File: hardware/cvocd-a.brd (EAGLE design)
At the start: 152.5 x 43.6 mm, 71 parts, among them IC1 PIC16F1825SO14, IC2 74HC595D, IC3 74HC595D, IC4 MCP4728_QUAD_DAC, IC5 LM324D, IC6 REG1117, IC7 6N138

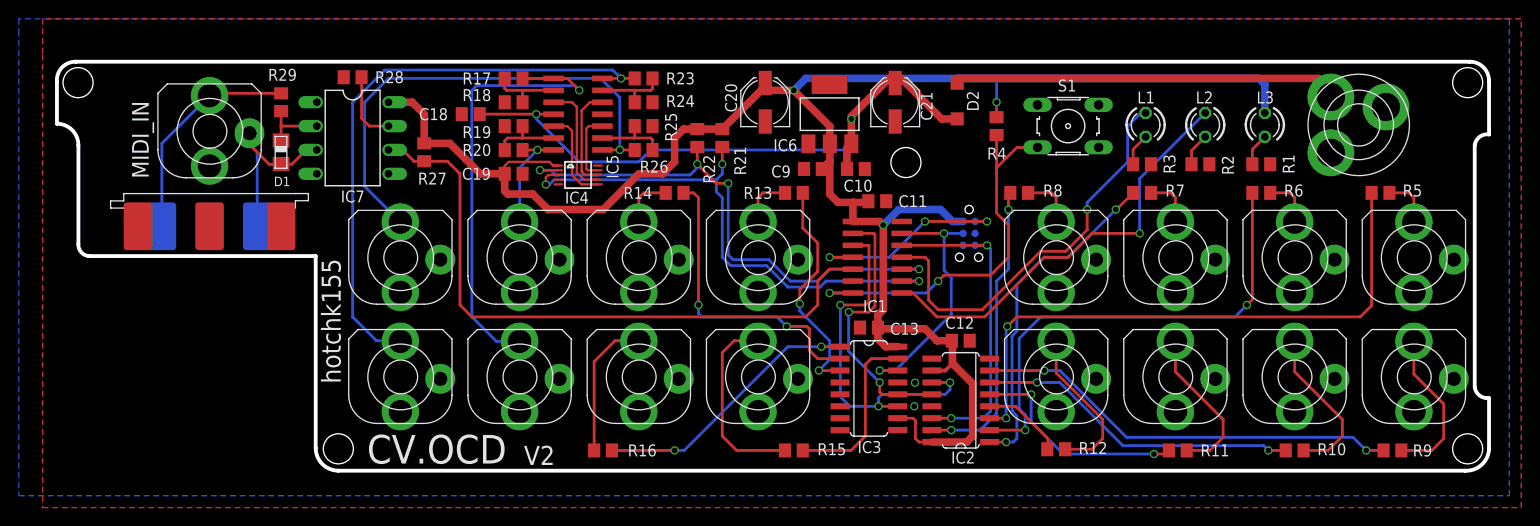
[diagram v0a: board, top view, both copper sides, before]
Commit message: icsp to top layer, current lim resistors
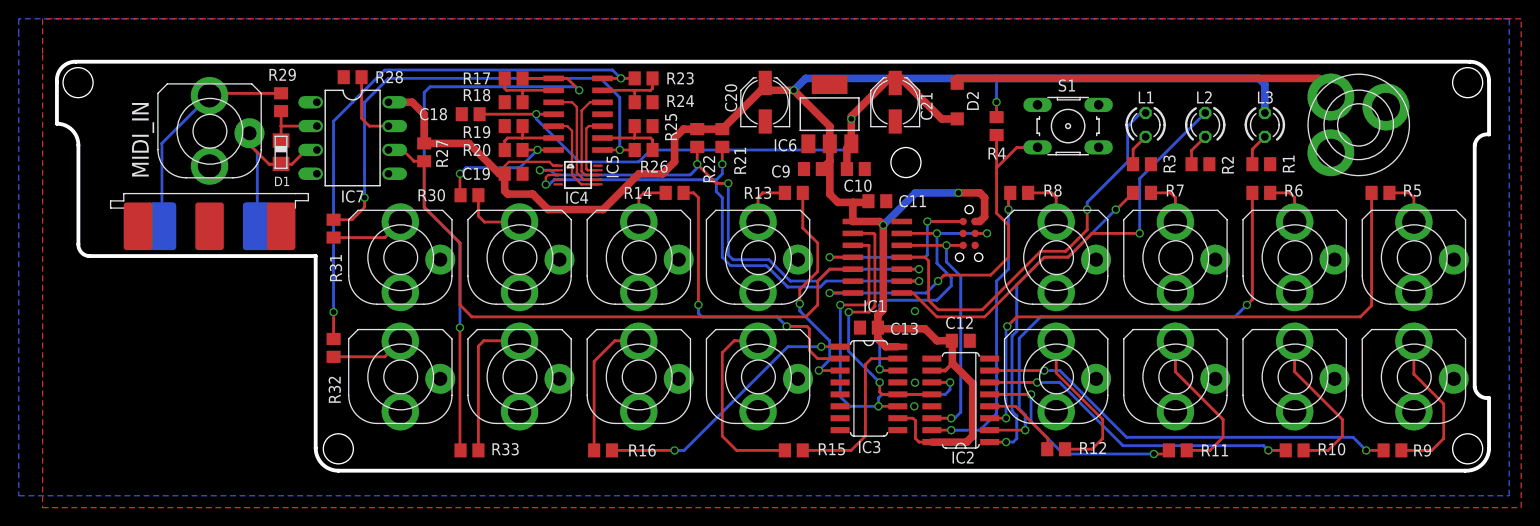
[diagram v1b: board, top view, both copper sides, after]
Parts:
- added R30, R31, R32, R33: 220r, rcl:R0805
- flipped ICSP to the top
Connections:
- new net N$10: CVD.4, R33.2
- new net N$11: CVB.4, R30.2
- new net N$14: CVA.4, R31.2
- new net N$17: CVC.4, R32.2
- net N$2: now also R33.1; no longer CVD.4
- net N$3: now also R30.1; no longer CVB.4
- net N$4: now also R31.1; no longer CVA.4
- net N$5: now also R32.1; no longer CVC.4
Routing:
- net N$10: track 0.00 -> 15.8 mm
- net N$2: track 48.7 -> 63.2 mm, vias 1 -> 2
- net N$17: track 0.00 -> 7.80 mm
- net N$14: track 0.00 -> 7.80 mm
- net N$11: track 0.00 -> 6.87 mm
- net SR_DAT2: track 34.7 -> 28.3 mm
- net SR_DAT: track 27.5 -> 33.9 mm, vias 2 -> 3
- net VDD: track 204.4 -> 210.4 mm, vias 3 -> 4
- net N$3: track 11.8 -> 14.9 mm, vias 1 -> 2
- net N$5: track 62.8 -> 59.9 mm, vias 1 -> 2
- net N$34: track 22.1 -> 20.4 mm, vias 3 -> 2
- net MIDI_IN: track 68.6 -> 67.2 mm
- net N$4: track 52.4 -> 53.1 mm, vias 1 -> 2
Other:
- board text added: "CC-NC-BY-SA"
- board text added: "V3"
- board text removed: "CV.OCD"
- board text removed: "V2"

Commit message: V3 possible final..
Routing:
- net N$33: track 16.9 -> 13.5 mm
- net GND: track 0.00 -> 3.11 mm, vias 3 -> 6
- net N$34: track 20.4 -> 19.8 mm
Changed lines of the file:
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@@
 </class>
 </classes>
-<designrules name="dirt_cheap_dirty_boards.v1">
-<description language="en">&lt;b&gt;Dirty Cheap Dirty Board Design Rules&lt;/b&gt;
-&lt;br&gt;
-&lt;br&gt;Min width/Spacing: 5/5mil
-&lt;br&gt;Min diameter of finished hole 12mil</description>
+<designrules name="hackvana">
+<description language="de">&lt;b&gt;EAGLE Design Rules für Hackvana&lt;/b&gt;
+&lt;p&gt;
+Die Standard-Design-Rules sind so gewählt, dass sie für
+die meisten Anwendungen passen. Sollte ihre Platine
+besondere Anforderungen haben, treffen Sie die erforderlichen
+Einstellungen hier und speichern die Design Rules unter
+einem neuen Namen ab.</description>
+<description language="en">&lt;b&gt;EAGLE Design Rules for Hackvana&lt;/b&gt;
+&lt;p&gt;
+The default Design Rules have been set to cover
+a wide range of applications. Your particular design
+may have different requirements, so please make the
+necessary adjustments and save your customized
+design rules under a new name.</description>
+<description language="zh">&lt;b&gt;EAGLE Design Rules for Hackvana&lt;/b&gt;
+</description>
 <param name="layerSetup" value="(1*16)"/>
-<param name="mtCopper" value="0.035mm 0.0175mm 0.035mm 0.035mm 0.035mm 0.035mm 0.035mm 0.035mm 0.035mm 0.035mm 0.035mm 0.035mm 0.035mm 0.035mm 0.0175mm 0.035mm"/>
-<param name="mtIsolate" value="1.5mm 1.1mm 0.2mm 0.15mm 0.2mm 0.15mm 0.2mm 0.15mm 0.2mm 0.15mm 0.2mm 0.15mm 0.2mm 0.15mm 0.2mm"/>
-<param name="mdWireWire" value="5mil"/>
-<param name="mdWirePad" value="5mil"/>
-<param name="mdWireVia" value="5mil"/>
-<param name="mdPadPad" value="5mil"/>
-<param name="mdPadVia" value="5mil"/>
-<param name="mdViaVia" value="5mil"/>
+<param name="mtCopper" value="0.035mm 0.035mm 0.035mm 0.035mm 0.035mm 0.035mm 0.035mm 0.035mm 0.035mm 0.035mm 0.035mm 0.035mm 0.035mm 0.035mm 0.035mm 0.035mm"/>
+<param name="mtIsolate" value="1.5mm 0.15mm 0.2mm 0.15mm 0.2mm 0.15mm 0.2mm 0.15mm 0.2mm 0.15mm 0.2mm 0.15mm 0.2mm 0.15mm 0.2mm"/>
+<param name="mdWireWire" value="6mil"/>
+<param name="mdWirePad" value="9mil"/>
+<param name="mdWireVia" value="6mil"/>
+<param name="mdPadPad" value="6mil"/>
+<param name="mdPadVia" value="6mil"/>
+<param name="mdViaVia" value="6mil"/>
 <param name="mdSmdPad" value="0mil"/>
 <param name="mdSmdVia" value="0mil"/>
@@
 <param name="mdViaViaSameLayer" value="8mil"/>
 <param name="mnLayersViaInSmd" value="2"/>
-<param name="mdCopperDimension" value="10mil"/>
-<param name="mdDrill" value="10mil"/>
+<param name="mdCopperDimension" value="6mil"/>
+<param name="mdDrill" value="6mil"/>
 <param name="mdSmdStop" value="0mil"/>
-<param name="msWidth" value="5mil"/>
-<param name="msDrill" value="12mil"/>
-<param name="msMicroVia" value="12mil"/>
+<param name="msWidth" value="6mil"/>
+<param name="msDrill" value="0.3mm"/>
+<param name="msMicroVia" value="0.25mm"/>
 <param name="msBlindViaRatio" value="0.5"/>
 <param name="rvPadTop" value="0.25"/>
@@
 <param name="mlMinCreamFrame" value="0mil"/>
 <param name="mlMaxCreamFrame" value="0mil"/>
-<param name="mlViaStopLimit" value="25mil"/>
+<param name="mlViaStopLimit" value="100mil"/>
 <param name="srRoundness" value="0"/>
 <param name="srMinRoundness" value="0mil"/>
@@
 <element name="U$2" library="jason_eagle6" package="PWR_SOCKET_2_1MM" value="PWR_SOCKET_2_1MM" x="138.905" y="35.687" smashed="yes" rot="R45"/>
 <element name="C21" library="rcl" package="PANASONIC_C" value="" x="89.535" y="38.1" smashed="yes" rot="R90">
-<attribute name="NAME" x="93.516" y="36.135" size="1.27" layer="25" rot="R90"/>
+<attribute name="NAME" x="93.77" y="36.77" size="1.27" layer="25" rot="R90"/>
 <attribute name="VALUE" x="93.31" y="35.45" size="1.016" layer="27" rot="R90"/>
 </element>
@@
 <via x="91.6432" y="8.2296" extent="1-16" drill="0.6"/>
 <via x="91.6432" y="15.8496" extent="1-16" drill="0.6"/>
+<via x="109.8042" y="1.6256" extent="1-16" drill="0.6"/>
+<via x="110.9472" y="1.6256" extent="1-16" drill="0.6"/>
+<via x="112.0902" y="1.6256" extent="1-16" drill="0.6"/>
+<wire x1="53.6399" y1="29.853" x2="54.729" y2="29.853" width="0.254" layer="1"/>
+<wire x1="54.729" y1="29.853" x2="54.864" y2="29.718" width="0.254" layer="1"/>
+<wire x1="54.864" y1="29.718" x2="54.864" y2="29.464" width="0.254" layer="1"/>
+<wire x1="57.8661" y1="31.353" x2="59.42" y2="31.353" width="0.254" layer="1"/>
+<wire x1="59.42" y1="31.353" x2="59.436" y2="31.369" width="0.254" layer="1"/>
 </signal>
 <signal name="N$1">
@@
 <contactref element="IC1" pad="4"/>
 <contactref element="ICSP" pad="1"/>
-<via x="92.964" y="25.4" extent="1-16" drill="0.6"/>
+<via x="95.504" y="25.4" extent="1-16" drill="0.6"/>
 <via x="82.55" y="21.59" extent="1-16" drill="0.6"/>
 <wire x1="82.55" y1="21.59" x2="85.03" y2="21.59" width="0.3048" layer="1"/>
 <wire x1="92.71" y1="21.59" x2="82.55" y2="21.59" width="0.3048" layer="16"/>
-<wire x1="92.964" y1="25.4" x2="96.774" y2="25.4" width="0.3048" layer="1"/>
-<wire x1="92.964" y1="25.4" x2="92.964" y2="21.844" width="0.3048" layer="16"/>
+<wire x1="95.504" y1="25.4" x2="96.774" y2="25.4" width="0.3048" layer="1"/>
 <wire x1="92.964" y1="21.844" x2="92.71" y2="21.59" width="0.3048" layer="16"/>
+<wire x1="92.964" y1="21.844" x2="92.964" y2="24.511" width="0.3048" layer="16"/>
+<wire x1="95.504" y1="25.4" x2="93.853" y2="25.4" width="0.3048" layer="16"/>
+<wire x1="93.853" y1="25.4" x2="92.964" y2="24.511" width="0.3048" layer="16"/>
 </signal>
 <signal name="N$35">
@@
 <contactref element="R4" pad="1"/>
 <contactref element="C20" pad="+"/>
-<wire x1="53.6399" y1="31.353" x2="53.229" y2="31.353" width="0.3048" layer="1"/>
-<wire x1="53.229" y1="31.353" x2="53.102" y2="31.353" width="0.254" layer="1"/>
 <wire x1="53.102" y1="31.353" x2="52.705" y2="31.75" width="0.254" layer="1"/>
 <wire x1="52.705" y1="31.75" x2="48.387" y2="31.75" width="0.254" layer="1"/>
@@
 <wire x1="88.265" y1="25.019" x2="91.694" y2="28.448" width="0.8128" layer="16"/>
 <wire x1="91.694" y1="28.448" x2="96.266" y2="28.448" width="0.8128" layer="16"/>
+<wire x1="53.102" y1="31.353" x2="53.6399" y2="31.353" width="0.254" layer="1"/>
 </signal>
 <signal name="VIN">
@@
 <contactref element="GATE9" pad="4"/>
 <wire x1="106.68" y1="12.64" x2="106.68" y2="9.271" width="0.3048" layer="1"/>
-<wire x1="106.68" y1="9.271" x2="111.633" y2="4.318" width="0.3048" layer="1"/>
-<wire x1="111.633" y1="4.318" x2="111.633" y2="2.286" width="0.3048" layer="1"/>
-<wire x1="111.633" y1="2.286" x2="110.49" y2="1.143" width="0.3048" layer="1"/>
-<wire x1="110.49" y1="1.143" x2="107.63" y2="1.143" width="0.3048" layer="1"/>
+<wire x1="106.68" y1="9.271" x2="109.601" y2="6.35" width="0.3048" layer="1"/>
+<wire x1="109.601" y1="6.35" x2="109.601" y2="3.114" width="0.3048" layer="1"/>
+<wire x1="109.601" y1="3.114" x2="107.63" y2="1.143" width="0.3048" layer="1"/>
 </signal>
 <signal name="N$39">

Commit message: working on v4
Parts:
- removed C10: (no value), rcl:C0805
- removed C18, C19, C9: 100n, rcl:C0805
- removed C20, C21: (no value), rcl:PANASONIC_C
- added C1, C4: 100n, rcl:C0805
- added C2, C3: (no value), rcl:PANASONIC_C
- added C5: (no value), rcl:C0805
- added PA, PB, PC, PD: (no value), rcl:RTRIM3314G
- IC1: value PIC16F1825SO14 -> 6N138; device jasons_stuff:SO14 -> optocoupler:DIL08
- IC2: value 74HC595D -> LM324D; device 74xx-eu:SO16 -> linear:SO14
- IC3: value 74HC595D -> MCP4728_QUAD_DAC; device 74xx-eu:SO16 -> jason_eagle6:MSOP10
- IC4: value MCP4728_QUAD_DAC -> REG1117; device jason_eagle6:MSOP10 -> burr-brown:SOT223
- IC5: value LM324D -> PIC16F1825SO14; device linear:SO14 -> jasons_stuff:SO14
- IC6: value REG1117 -> 74HC595D; device burr-brown:SOT223 -> 74xx-eu:SO16
- IC7: value 6N138 -> 74HC595D; device optocoupler:DIL08 -> 74xx-eu:SO16
- R10, R11, R8, R9: value (none) -> 220r
- R12, R13, R14, R15, R5, R6, R7: value (none) -> 100k
- R17, R18, R19, R23, R24, R25, R26: value 100k -> (none)
- R2, R3: value (none) -> 1k5
- R20: value 100k -> 4k7
- R22: value 4k7 -> 10k
- R27, R28: value 1k5 -> (none)
- R30, R31, R32, R33: value 220r -> (none)
- R4: value 10k -> 100k
- moved R1 119.8 mm to (8.89, 38.1), turned to 270 degrees
- moved R29 117.5 mm to (141.2, 28.4), turned to 0 degrees
- moved R32 102.9 mm to (132.1, 1.02), turned to 0 degrees
- moved R9 98.3 mm to (49.9, 34.2), turned to 90 degrees
- moved R33 98.3 mm to (142.5, 1.02)
- moved R28 97.6 mm to (128.5, 28.4), turned to 0 degrees
- moved R2 96.2 mm to (26.3, 40.6), turned to 180 degrees
- moved R5 95.1 mm to (46.6, 38.2)
- moved R31 93.0 mm to (119.6, 1.02), turned to 0 degrees
- moved R3 84.2 mm to (32.1, 40.6)
- moved R6 82.2 mm to (46.6, 35.3), turned to 180 degrees
- moved R10 80.1 mm to (61.7, 39.2), turned to 270 degrees
- moved R27 76.6 mm to (115.8, 28.4), turned to 0 degrees
- moved IC7 70.5 mm to (96.5, 6.35), turned to 90 degrees
- moved R7 69.4 mm to (46.6, 32.9)
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- renumbered C11 to C6, C12 to C8, C13 to C7, L1 to LED1, L2 to LED2, L3 to LED3, S1 to SW1
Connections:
- removed net N$3 (its old number): IC5.7, R20.2, R30.1
- new net N$18: CVD.4, R5.2, R8.2
- new net N$19: CVB.4, R7.2, R9.2
- new net N$38: CVA.4, R11.2, R14.2
- new net N$44: CVC.4, R10.2, R12.2
- new net N$45: PA.1, R15.2
- new net N$53: IC7.7, R33.1
- new net N$54: PA.3, R14.1
- new net N$55: PC.1, R13.2
- new net N$56: PC.3, R12.1
- net ACT_LED: now also IC5.11; no longer IC1.11
- net GND: now also C1.1, C2.-, C3.-, C4.1, C5.1, IC1.5, IC2.11, IC3.10, IC3.4, IC4.1, IC5.14, IC6.13, IC6.8, IC7.13, IC7.8, R13.1, R15.1, R23.2, R24.2, R25.2, R4.1, R6.1; no longer C10.1, C18.2, C19.1, C20.-, C21.-, C9.1, IC1.14, IC2.13, IC2.8, IC3.13, IC3.8, IC4.10, IC4.4, IC5.11, IC6.1, IC7.5, R1.2, R18.1, R19.1, R2.2, R24.1, R25.1, R28.2
- net MIDI_IN: now also IC1.6, IC5.5, R2.1; no longer IC1.5, IC7.6, R27.1
- net MIDI_OUT: now also IC5.6; no longer IC1.6
- net N$1: now also R19.2; no longer R15.2
- net N$10: now also IC2.2, PD.2; no longer CVD.4, R33.2
- net N$11: now also IC2.9, PA.2; no longer CVB.4, R30.2
- net N$12: now also IC6.15, R19.1; no longer IC3.15, R15.1
- net N$13: now also IC6.1, R18.1; no longer IC3.1, R16.1
- net N$14: now also IC2.13, PC.2; no longer CVA.4, R31.2
- net N$15: now also IC6.3, R17.1; no longer IC3.3, R13.1
- net N$16: now also IC6.2, R16.1; no longer IC3.2, R14.1
- net N$17: now also PD.1, R4.2; no longer CVC.4, R32.2
- net N$2: now also IC2.1, R8.1; no longer IC5.1, R17.2, R33.1
- net N$20: now also R26.2; no longer R8.2
- net N$21: now also IC3.2, IC5.10, R21.2; no longer IC1.10, IC4.2, R22.2
- net N$22: now also IC3.3, IC5.9, R20.2; no longer IC1.9, IC4.3, R21.2
- net N$23: now also R27.2; no longer R7.2
- net N$24: now also R28.2; no longer R6.2
- net N$25: now also PD.3, R5.1; no longer IC5.2, R17.1, R18.2
- net N$26: now also IC2.6, PB.2; no longer IC5.6, R19.2, R20.1
- net N$27: now also PB.1, R6.2; no longer IC5.9, R25.2, R26.1
- net N$28: now also PB.3, R7.1; no longer IC5.13, R23.1, R24.2
- net N$29: now also R1.1; no longer R29.1
- net N$30: now also IC1.2, R1.2; no longer IC7.2, R29.2
- net N$31: now also IC1.3; no longer IC7.3
- net N$32: now also R29.2; no longer R5.2
- net N$33: now also R30.2; no longer R12.2
- net N$34: now also IC5.4; no longer IC1.4
- net N$35: now also R25.1; no longer R1.1
- net N$36: now also R23.1; no longer R3.1
- net N$37: now also R24.1; no longer R2.1
- net N$39: now also R31.2; no longer R11.2
- net N$4: now also IC2.8, R11.1; no longer IC5.8, R26.2, R31.1
- net N$41: now also R32.2; no longer R10.2
- net N$42: now also IC1.7, R3.1; no longer IC7.7, R28.1
- net N$43: now also IC7.15, R26.1; no longer IC2.15, R8.1
- net N$46: now also IC7.1, R27.1; no longer IC2.1, R7.1
- net N$47: now also IC7.3, R29.1; no longer IC2.3, R5.1
- net N$48: now also IC7.2, R28.1; no longer IC2.2, R6.1
- net N$49: now also IC7.5, R31.1; no longer IC2.5, R11.1
- net N$5: now also IC2.14, R10.1; no longer IC5.14, R23.2, R32.1
- net N$50: now also IC7.6, R32.1; no longer IC2.6, R10.1
- net N$51: now also IC7.4, R30.1; no longer IC2.4, R12.1
- net N$52: now also R33.2; no longer R9.2
- net N$6: now also R18.2; no longer R16.2
- net N$7: now also R16.2; no longer R14.2
- net N$8: now also R17.2; no longer R13.2
- net N$9: now also IC5.7, R22.2; no longer IC1.7, R4.2
- net SR_CLK: now also IC5.3, IC6.11, IC7.11; no longer IC1.3, IC2.11, IC3.11
- net SR_DAT: now also IC5.13, IC6.14; no longer IC1.13, IC3.14
- net SR_DAT2: now also IC5.12, IC7.14; no longer IC1.12, IC2.14
- net SR_RCK: now also IC5.2, IC6.12, IC7.12; no longer IC1.2, IC2.12, IC3.12
- net STATUS_LED: now also IC5.8; no longer IC1.8
- net VDD: now also C1.2, C2.+, C4.2, IC1.8, IC3.1, IC4.2, IC5.1, IC6.10, IC6.16, IC7.10, IC7.16, R2.2, R20.1; no longer C19.2, C20.+, C9.2, IC1.1, IC2.10, IC2.16, IC3.10, IC3.16, IC4.1, IC6.2, IC7.8, R27.2, R4.1
- net VIN: now also C3.+, C5.2, IC2.4, IC4.3; no longer C10.2, C18.1, C21.+, IC5.4, IC6.3
- net VOUTA: now also IC2.5, IC3.6; no longer IC4.6, IC5.5
- net VOUTB: now also IC2.3, IC3.7; no longer IC4.7, IC5.3
- net VOUTC: now also IC2.12, IC3.8; no longer IC4.8, IC5.12
- net VOUTD: now also IC2.10, IC3.9; no longer IC4.9, IC5.10
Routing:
- net N$44: track 0.00 -> 63.6 mm, vias 0 -> 2
- net N$2: track 63.2 -> 3.50 mm, vias 2 -> 0
- net N$5: track 59.9 -> 3.48 mm, vias 2 -> 0
- net N$38: track 0.00 -> 54.4 mm, vias 0 -> 1
- net N$4: track 53.1 -> 3.40 mm, vias 2 -> 0
- net N$53: track 0.00 -> 45.5 mm, vias 0 -> 2
- net N$3: track 45.5 -> 3.31 mm, vias 2 -> 0
- net N$18: track 0.00 -> 40.4 mm, vias 0 -> 1
- net MIDI_IN: track 67.2 -> 93.2 mm
- net N$19: track 0.00 -> 17.7 mm
- net N$30: track 6.94 -> 23.0 mm
- net N$3 (its old number): track 14.9 -> 0.00 mm, vias 2 -> 0
- net N$40: track 41.5 -> 32.6 mm
- net N$11: track 6.87 -> 15.6 mm, vias 0 -> 2
- net N$21: track 57.1 -> 65.1 mm, vias 4 -> 3
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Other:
- board text added: "CV.OCD"
- board text added: "V4"
- board text removed: "V3"

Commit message: REV4 RELEASE CANDIDATE
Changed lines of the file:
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@@
 </element>
 <element name="R17" library="rcl" package="R0805" value="" x="78.74" y="28.448" smashed="yes" rot="R180">
-<attribute name="NAME" x="76.708" y="29.464" size="1.27" layer="25" rot="R180"/>
+<attribute name="NAME" x="76.581" y="29.21" size="1.27" layer="25" rot="R180"/>
 <attribute name="VALUE" x="79.375" y="30.988" size="1.27" layer="27" rot="R180"/>
 </element>
@@
 </element>
 <element name="R21" library="rcl" package="R0805" value="4k7" x="78.74" y="30.734" smashed="yes" rot="R180">
-<attribute name="NAME" x="76.835" y="31.115" size="1.27" layer="25" rot="R180"/>
+<attribute name="NAME" x="76.708" y="30.988" size="1.27" layer="25" rot="R180"/>
 </element>
 <element name="R20" library="rcl" package="R0805" value="4k7" x="78.74" y="33.02" smashed="yes" rot="R180">
-<attribute name="NAME" x="76.835" y="32.766" size="1.27" layer="25" rot="R180"/>
+<attribute name="NAME" x="75.184" y="34.798" size="1.27" layer="25" rot="R270"/>
 </element>
 <element name="IC2" library="linear" package="SO14" value="LM324D" x="55.753" y="36.83" smashed="yes" rot="R270">
@@
 </element>
 <element name="R8" library="rcl" package="R0805" value="220r" x="49.911" y="39.243" smashed="yes" rot="R270">
-<attribute name="NAME" x="46.101" y="31.115" size="1.016" layer="25" rot="R270"/>
+<attribute name="NAME" x="46.228" y="31.242" size="1.016" layer="25" rot="R270"/>
 </element>
 <element name="R9" library="rcl" package="R0805" value="220r" x="49.911" y="34.163" smashed="yes" rot="R90">
-<attribute name="NAME" x="46.99" y="27.305" size="1.016" layer="25" rot="R90"/>
+<attribute name="NAME" x="46.99" y="27.432" size="1.016" layer="25" rot="R90"/>
 </element>
 <element name="R11" library="rcl" package="R0805" value="220r" x="61.722" y="34.163" smashed="yes" rot="R90">
-<attribute name="NAME" x="59.182" y="29.464" size="1.016" layer="25" rot="R270"/>
+<attribute name="NAME" x="59.182" y="29.718" size="1.016" layer="25" rot="R270"/>
 </element>
 <element name="R10" library="rcl" package="R0805" value="220r" x="61.722" y="39.243" smashed="yes" rot="R270">
-<attribute name="NAME" x="60.198" y="29.718" size="1.016" layer="25" rot="R90"/>
+<attribute name="NAME" x="59.817" y="29.718" size="1.016" layer="25" rot="R90"/>
 </element>
 <element name="PC" library="rcl" package="RTRIM3314G" value="" x="71.12" y="39.243" smashed="yes" rot="R270">

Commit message: v5 board first version
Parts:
- removed PA, PB, PC, PD: (no value), rcl:RTRIM3314G
- added C10, C11, C12, C9: 22p, rcl:C0805
- moved R4 5.39 mm to (41.4, 39.2), turned to 90 degrees
- moved R6 5.28 mm to (41.4, 34.4), turned to 270 degrees
- moved R15 4.94 mm to (69.8, 34.4), turned to 270 degrees
- moved R13 4.81 mm to (69.8, 39.2), turned to 90 degrees
- moved R7 3.18 mm to (43.8, 34.4), turned to 90 degrees
- moved R5 2.97 mm to (43.8, 39.2), turned to 270 degrees
- moved R9 2.81 mm to (47.1, 34.4)
- moved R8 2.79 mm to (47.1, 39.2)
- moved R12 2.79 mm to (67.6, 39.2), turned to 270 degrees
- moved R14 2.57 mm to (67.6, 34.4), turned to 90 degrees
- moved R11 2.55 mm to (64.3, 34.4)
- moved R10 2.54 mm to (64.3, 39.2)
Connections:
- removed net N$17: PD.1, R4.2
- removed net N$25: PD.3, R5.1
- removed net N$27: PB.1, R6.2
- removed net N$28: PB.3, R7.1
- removed net N$45: PA.1, R15.2
- removed net N$54: PA.3, R14.1
- removed net N$55: PC.1, R13.2
- removed net N$56: PC.3, R12.1
- net N$10: now also C9.2, R4.2, R5.1; no longer PD.2
- net N$11: now also C11.2, R14.1, R15.2; no longer PA.2
- net N$14: now also C12.2, R12.1, R13.2; no longer PC.2
- net N$2: now also C9.1
- net N$26: now also C10.2, R6.2, R7.1; no longer PB.2
- net N$3: now also C10.1
- net N$4: now also C11.1
- net N$5: now also C12.1
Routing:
- net N$38: track 54.4 -> 41.5 mm, vias 1 -> 0
- net N$44: track 63.6 -> 69.2 mm
- net N$11: track 15.6 -> 20.7 mm
- net N$18: track 40.4 -> 35.7 mm, vias 1 -> 3
- net N$4: track 3.40 -> 7.23 mm
- net N$3: track 3.31 -> 6.84 mm
- net N$5: track 3.48 -> 6.76 mm
- net N$2: track 3.50 -> 6.57 mm
- net N$17: track 2.50 -> 0.00 mm
- net N$25: track 2.45 -> 0.00 mm
- net N$28: track 2.45 -> 0.00 mm
- net N$27: track 2.40 -> 0.00 mm
- net N$56: track 2.37 -> 0.00 mm
- net N$55: track 2.32 -> 0.00 mm
- net N$45: track 2.32 -> 0.00 mm
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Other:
- board text added: "V5"
- board text removed: "V4"
